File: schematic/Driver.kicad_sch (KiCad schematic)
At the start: 0 parts

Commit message: Create driver schematic
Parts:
- added C18: Tune, symbol Device:C
- added C19, C20, C21: 1uF, symbol Device:C
- added C22, C23, C24: 100uF, symbol Device:C
- added D2, D3: 1N5819, Diode_THT:D_DO-41_SOD81_P10.16mm_Horizontal, symbol Diode:1N5819
- added D4, D5: 1N5349, symbol Device:D_Zener
- added D6, D7: 1N5352, symbol Device:D_Zener
- added Q1, Q2, Q3: IRFZ44N, IRFZ44N:TO254P1016X419X2286-3, symbol IRFZ44N:IRFZ44N
- added R6: 200R, symbol Device:R
- added RV1: 1k, symbol Device:R_Potentiometer
- added T1: 1:1, symbol Device:Transformer_1P_1S
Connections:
- net A: now also Q2.2
- net B: now also Q3.2
- net Base: now also C18.1, T1.2 (AB)
- net Signal: now also Q1.1
- new net: D5.1 (K), D6.1 (K)
- new net: D3.2 (A), D5.2 (A), Q3.1, R6.1, T1.3 (SA)
- new net: D2.1 (K), D3.1 (K), Q1.2
- new net: D2.2 (A), D4.2 (A), Q2.1, T1.4 (SB)
- new net: R6.2, RV1.2
- new net: D4.1 (K), D7.1 (K)
- new net +24V: C19.1, C20.1, C21.1, C22.1, C23.1, C24.1
- new net +5V: RV1.3
- new net GND: C18.2, C19.2, C20.2, C21.2, C22.2, C23.2, C24.2, D6.2 (A), D7.2 (A), Q1.3, Q2.3, Q3.3, RV1.1, T1.1 (AA)

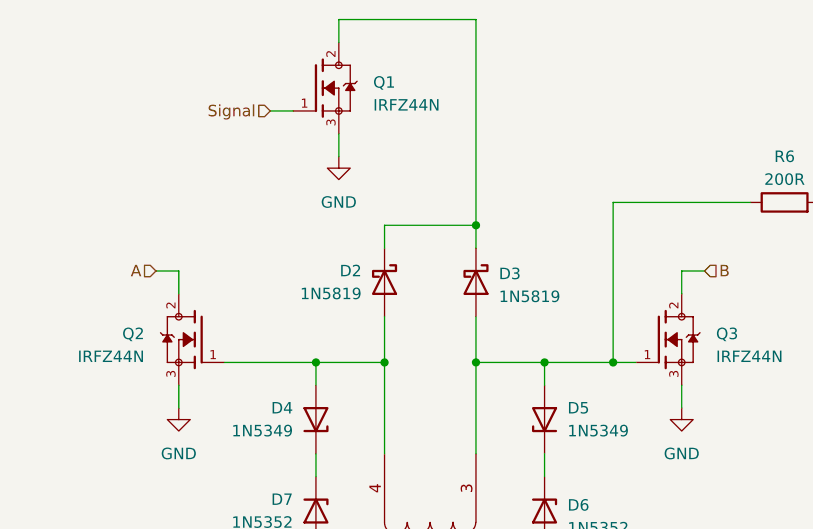
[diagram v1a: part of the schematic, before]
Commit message: Add test points to driver signals
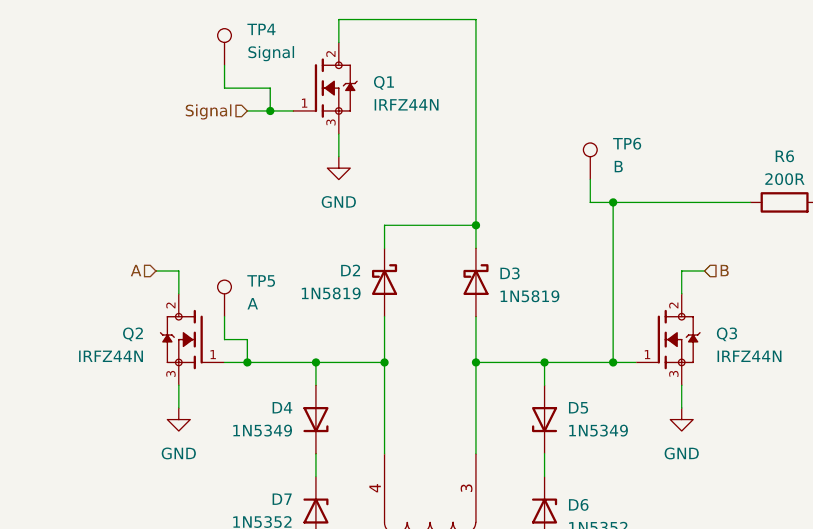
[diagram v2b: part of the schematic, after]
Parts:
- added TP4: Signal, symbol Connector:TestPoint
- added TP5: A, symbol Connector:TestPoint
- added TP6: B, symbol Connector:TestPoint
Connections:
- net Signal: now also TP4.1
- net at D3.2 (A), D5.2 (A), Q3.1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: now also TP6.1
- net at D2.2 (A), D4.2 (A), Q2.1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: now also TP5.1

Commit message: Assign footprints
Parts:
- C18, C19, C20, C21: footprint (none) -> Capacitor_SMD:C_0603_1608Metric
- C22, C23, C24: footprint (none) -> Capacitor_THT:CP_Radial_D8.0mm_P3.80mm
- D4, D5, D6, D7: footprint (none) -> Diode_THT:D_DO-41_SOD81_P10.16mm_Horizontal
- R6: footprint (none) -> Resistor_SMD:R_0603_1608Metric
- RV1: footprint (none) -> Potentiometer_THT:Potentiometer_Runtron_RM-065_Vertical
- T1: footprint (none) -> Inductor_THT:L_Toroid_Vertical_L26.7mm_W14.0mm_P10.16mm_Pulse_D
- TP4, TP5, TP6: footprint (none) -> TestPoint:TestPoint_Pad_D2.0mm
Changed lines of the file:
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@@
       (effects (font (size 1.27 1.27)) (justify right))
     )
-    (property "Footprint" "" (at 160.02 95.25 0)
+    (property "Footprint" "Diode_THT:D_DO-41_SOD81_P10.16mm_Horizontal" (at 160.02 95.25 0)
       (effects (font (size 1.27 1.27)) hide)
     )
@@
       (effects (font (size 1.27 1.27)) (justify left))
     )
-    (property "Footprint" "" (at 102.5652 129.54 0)
+    (property "Footprint" "Capacitor_SMD:C_0603_1608Metric" (at 102.5652 129.54 0)
       (effects (font (size 1.27 1.27)) hide)
     )
@@
       (effects (font (size 1.27 1.27)) (justify left))
     )
-    (property "Footprint" "" (at 115.2652 129.54 0)
+    (property "Footprint" "Capacitor_SMD:C_0603_1608Metric" (at 115.2652 129.54 0)
       (effects (font (size 1.27 1.27)) hide)
     )
@@
       (effects (font (size 1.27 1.27)) (justify left))
     )
-    (property "Footprint" "" (at 129.54 83.82 0)
+    (property "Footprint" "TestPoint:TestPoint_Pad_D2.0mm" (at 129.54 83.82 0)
       (effects (font (size 1.27 1.27)) hide)
     )
@@
       (effects (font (size 1.27 1.27)) (justify left))
     )
-    (property "Footprint" "" (at 89.8652 129.54 0)
+    (property "Footprint" "Capacitor_SMD:C_0603_1608Metric" (at 89.8652 129.54 0)
       (effects (font (size 1.27 1.27)) hide)
     )
@@
       (effects (font (size 1.27 1.27)) (justify left))
     )
-    (property "Footprint" "" (at 204.1652 129.54 0)
+    (property "Footprint" "Capacitor_THT:CP_Radial_D8.0mm_P3.80mm" (at 204.1652 129.54 0)
       (effects (font (size 1.27 1.27)) hide)
     )
@@
       (effects (font (size 1.27 1.27)))
     )
-    (property "Footprint" "" (at 186.69 72.898 90)
+    (property "Footprint" "Resistor_SMD:R_0603_1608Metric" (at 186.69 72.898 90)
       (effects (font (size 1.27 1.27)) hide)
     )
@@
       (effects (font (size 1.27 1.27)) (justify left))
     )
-    (property "Footprint" "" (at 170.18 68.58 0)
+    (property "Footprint" "TestPoint:TestPoint_Pad_D2.0mm" (at 170.18 68.58 0)
       (effects (font (size 1.27 1.27)) hide)
     )
@@
       (effects (font (size 1.27 1.27)) (justify right))
     )
-    (property "Footprint" "" (at 147.32 109.22 0)
+    (property "Footprint" "Inductor_THT:L_Toroid_Vertical_L26.7mm_W14.0mm_P10.16mm_Pulse_D" (at 147.32 109.22 0)
       (effects (font (size 1.27 1.27)) hide)
     )
@@
       (effects (font (size 1.27 1.27)) (justify right))
     )
-    (property "Footprint" "" (at 134.62 95.25 0)
+    (property "Footprint" "Diode_THT:D_DO-41_SOD81_P10.16mm_Horizontal" (at 134.62 95.25 0)
       (effects (font (size 1.27 1.27)) hide)
     )
@@
       (effects (font (size 1.27 1.27)) (justify left))
     )
-    (property "Footprint" "" (at 191.4652 129.54 0)
+    (property "Footprint" "Capacitor_THT:CP_Radial_D8.0mm_P3.80mm" (at 191.4652 129.54 0)
       (effects (font (size 1.27 1.27)) hide)
     )
@@
       (effects (font (size 1.27 1.27)) (justify right))
     )
-    (property "Footprint" "" (at 134.62 105.41 0)
+    (property "Footprint" "Diode_THT:D_DO-41_SOD81_P10.16mm_Horizontal" (at 134.62 105.41 0)
       (effects (font (size 1.27 1.27)) hide)
     )
@@
       (effects (font (size 1.27 1.27)) (justify left))
     )
-    (property "Footprint" "" (at 153.3652 132.08 0)
+    (property "Footprint" "Capacitor_SMD:C_0603_1608Metric" (at 153.3652 132.08 0)
       (effects (font (size 1.27 1.27)) hide)
     )
@@
       (effects (font (size 1.27 1.27)) (justify left))
     )
-    (property "Footprint" "" (at 129.54 55.88 0)
+    (property "Footprint" "TestPoint:TestPoint_Pad_D2.0mm" (at 129.54 55.88 0)
       (effects (font (size 1.27 1.27)) hide)
     )
@@
       (effects (font (size 1.27 1.27)) (justify left))
     )
-    (property "Footprint" "" (at 160.02 105.41 0)
+    (property "Footprint" "Diode_THT:D_DO-41_SOD81_P10.16mm_Horizontal" (at 160.02 105.41 0)
       (effects (font (size 1.27 1.27)) hide)
     )
@@
       (effects (font (size 1.27 1.27)) (justify right))
     )
-    (property "Footprint" "" (at 196.85 71.12 0)
+    (property "Footprint" "Potentiometer_THT:Potentiometer_Runtron_RM-065_Vertical" (at 196.85 71.12 0)
       (effects (font (size 1.27 1.27)) hide)
     )
@@
       (effects (font (size 1.27 1.27)) (justify left))
     )
-    (property "Footprint" "" (at 178.7652 129.54 0)
-      (effects (font (size 1.27 1.27)) hide)
-    )
+    (property "Footprint" "Capacitor_THT:CP_Radial_D8.0mm_P3.80mm" (at 178.7652 129.54 0)
+      (effects (font (size 1.27 1.27)) hide)
+    )

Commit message: Fix driver transformer footprint
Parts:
- T1: footprint Inductor_THT:L_Toroid_Vertical_L26.7mm_W14.0mm_P10.16mm_Pulse_D -> Transformer_THT:Transformer_Toroid_Horizontal_D9.0mm_Amidon-T30
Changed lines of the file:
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@@
       (effects (font (size 1.27 1.27)) (justify right))
     )
-    (property "Footprint" "Inductor_THT:L_Toroid_Vertical_L26.7mm_W14.0mm_P10.16mm_Pulse_D" (at 147.32 109.22 0)
+    (property "Footprint" "Transformer_THT:Transformer_Toroid_Horizontal_D9.0mm_Amidon-T30" (at 147.32 109.22 0)
       (effects (font (size 1.27 1.27)) hide)
     )

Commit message: Design PCB
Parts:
- added C19, C20: Tune, Capacitor_SMD:C_0603_1608Metric, symbol Device:C
- renumbered C19 to C21, C20 to C22, C21 to C23, C22 to C24, C23 to C25, C24 to C26, D7 to D6, D6 to D7
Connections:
- net Base: now also C19.1, C20.1
- net GND: now also C19.2, C20.2
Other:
- moved on the sheet: C18
